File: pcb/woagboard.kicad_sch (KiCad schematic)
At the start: 54 parts, among them J1 TYPE-C-31-M-12, J2 SWD, J3 TC2030, SW1 SW_Push_45deg, SW10 SW_Push_45deg, SW11 SW_Push_45deg, SW12 SW_Push_45deg, SW13 SW_Push_45deg, SW14 SW_Push_45deg, SW15 SW_Push_45deg, SW16 SW_Push_45deg, SW17 SW_Push_45deg, SW18 SW_Push_45deg, SW2 SW_Push_45deg, SW3 SW_Push_45deg, SW4 SW_Push_45deg, SW5 SW_Push_45deg, SW6 SW_Push_45deg, SW7 SW_Push_45deg, SW8 SW_Push_45deg, SW9 SW_Push_45deg, U1 E73-2G4M08S1C, U2 BQ24075RGT, U3 USBLC6-2, Y1 32.768kHz

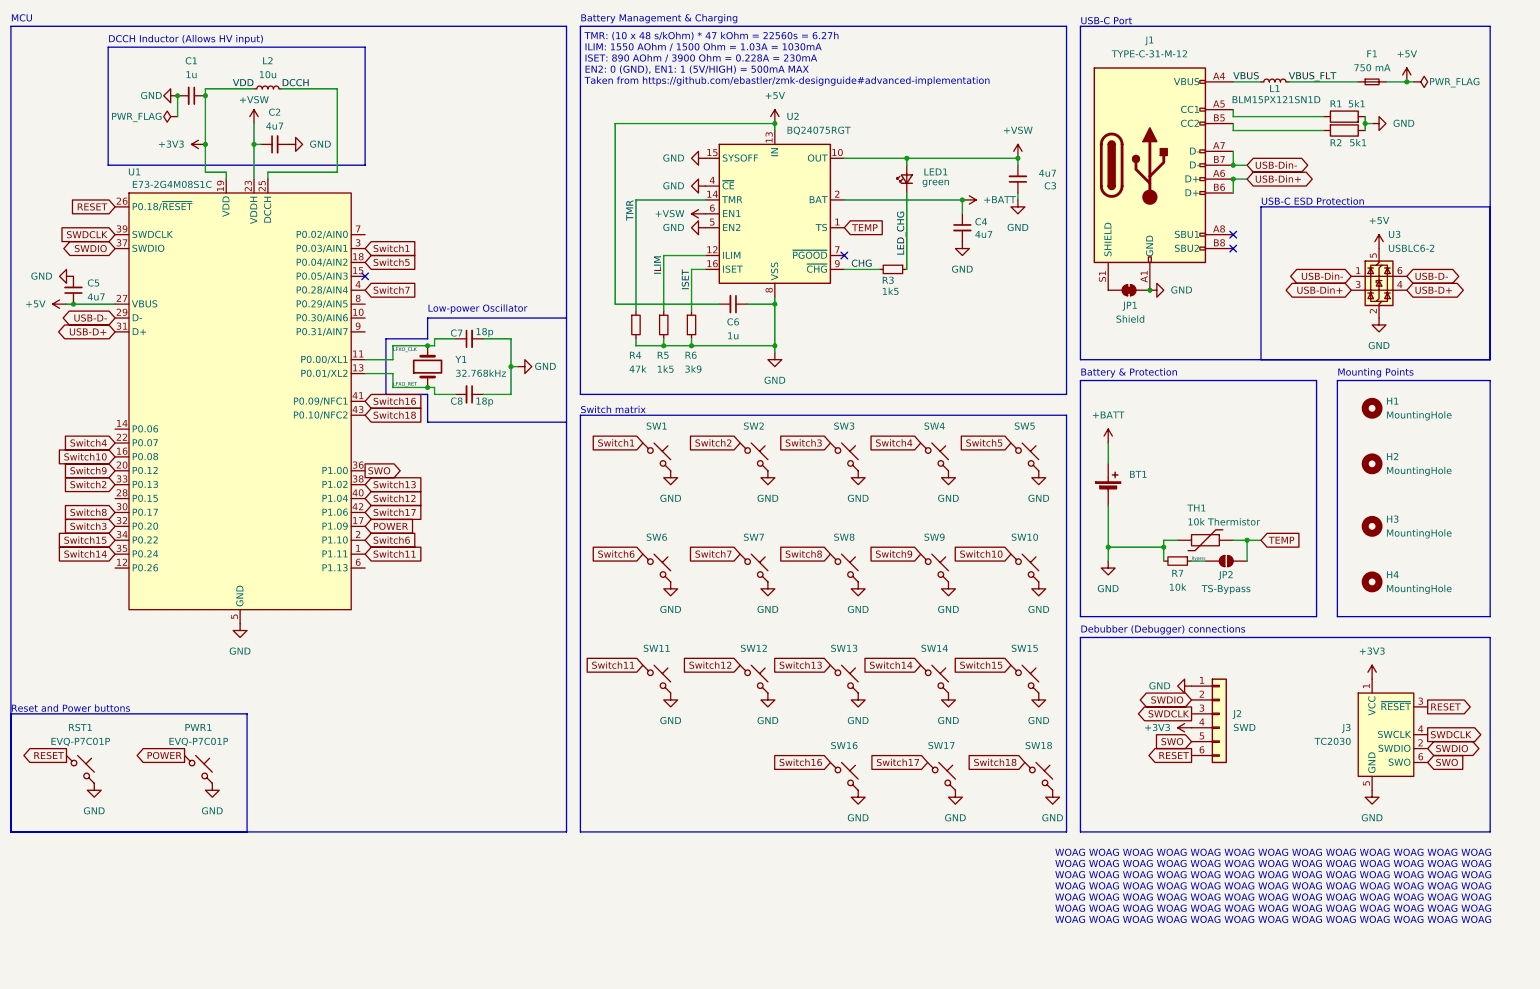
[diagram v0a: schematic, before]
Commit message: feat: reorganise and add basic case files
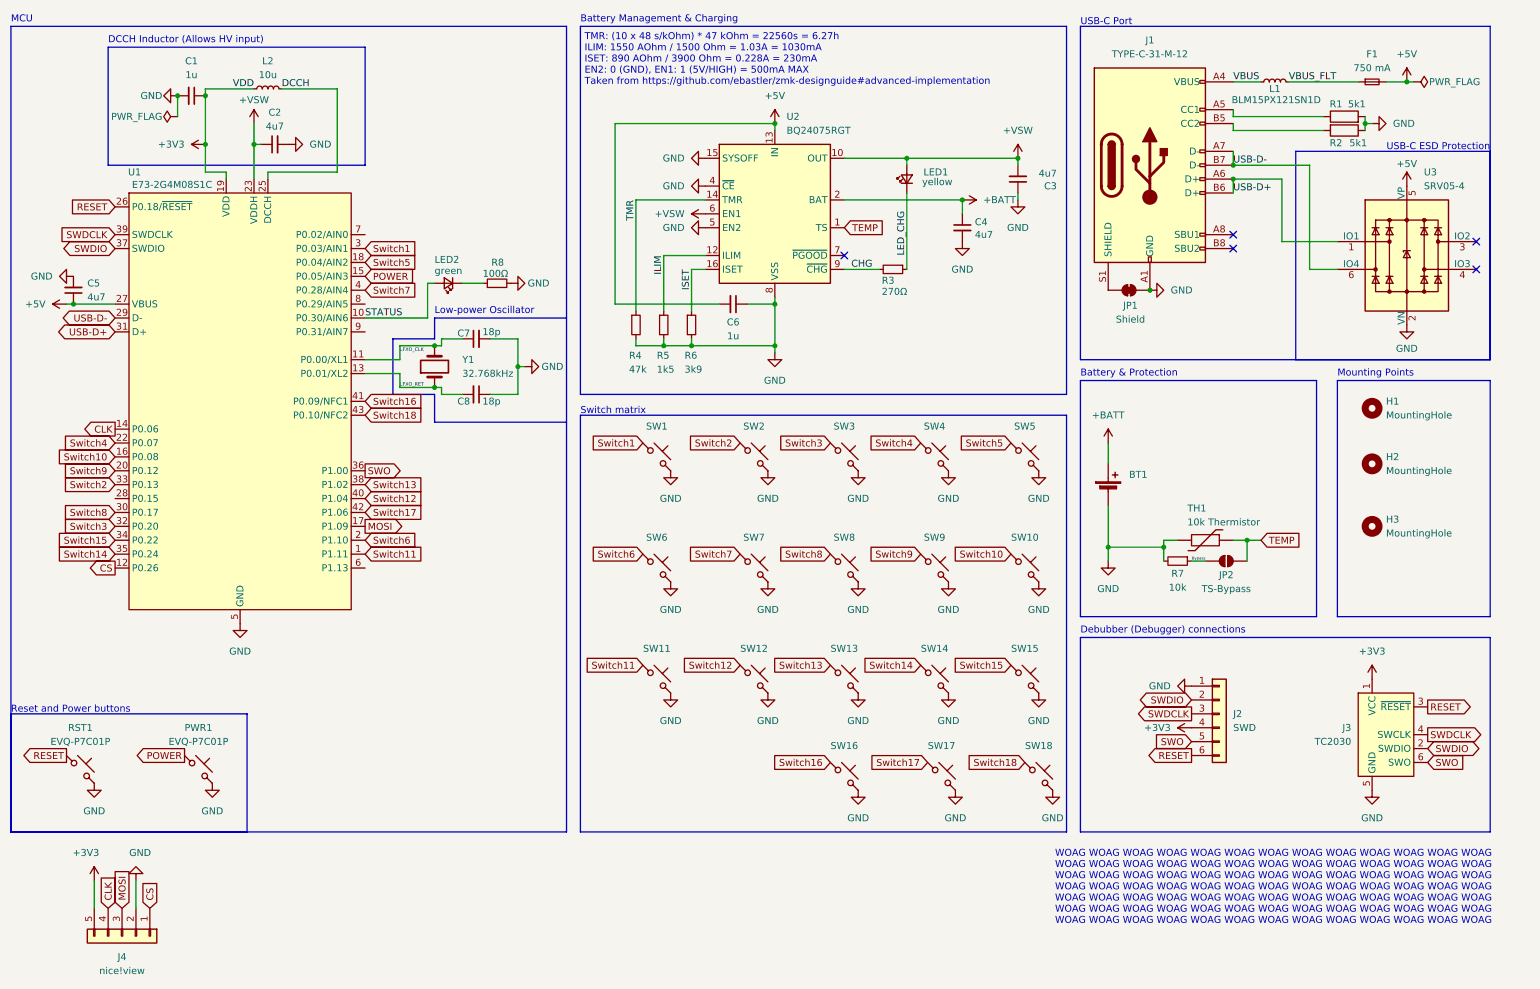
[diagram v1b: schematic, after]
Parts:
- removed H4: MountingHole, MountingHole:MountingHole_2.2mm_M2, symbol Mechanical:MountingHole
- removed U3: USBLC6-2, Package_TO_SOT_SMD:SOT-23-6_Handsoldering, symbol Power_Protection:USBLC6-2P6
- added J4: nice!view, Woagboard_Footprints:nice!view_pads, symbol Connector_Generic:Conn_01x05
- added LED2: green, LED_SMD:LED_0805_2012Metric_Pad1.15x1.40mm_HandSolder, symbol Device:LED_Small
- added R8: 100Ω, Resistor_SMD:R_0603_1608Metric_Pad0.98x0.95mm_HandSolder, symbol Device:R_Small
- added U3: SRV05-4, PCM_marbastlib-various:SOT-23-6-routable, symbol PCM_marbastlib-various:SRV05-4
- BT1, SW1, SW10, SW11, SW12, SW13, SW14, SW15, SW16, SW17, SW18, SW2, SW3, SW4, SW5, SW6, SW7, SW8, SW9: now left out of the parts list
- C1: LCSC (none) -> C52923
- C2, C5: LCSC (none) -> C23733
- C3, C4: LCSC C1538 -> C23733
- C7, C8: LCSC (none) -> C1549
- J1: LCSC (none) -> C165948
- J2: LCSC (none) -> C706869
- L2: LCSC (none) -> C223249
- LED1: value green -> yellow; footprint LED_SMD:LED_0603_1608Metric_Pad1.05x0.95mm_HandSolder -> LED_SMD:LED_0805_2012Metric_Pad1.15x1.40mm_HandSolder; LCSC C2290 -> C2296
- PWR1, RST1: LCSC (none) -> C388883
- R3: value 1k5 -> 270Ω; footprint Resistor_SMD:R_0402_1005Metric_Pad0.72x0.64mm_HandSolder -> Resistor_SMD:R_0603_1608Metric_Pad0.98x0.95mm_HandSolder
- U2: footprint Package_DFN_QFN:VQFN-16-1EP_3x3mm_P0.5mm_EP1.6x1.6mm -> Package_DFN_QFN:QFN-16-1EP_3x3mm_P0.5mm_EP1.7x1.7mm
- Y1: LCSC (none) -> C32346
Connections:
- net USB-Din+ is gone; now on net USB-D+: J1.A6 (D+), J1.B6 (D+)
- net USB-Din- is gone; now on net USB-D-: J1.A7 (D-), J1.B7 (D-)
- net +3V3: now also J4.5 (Pin_5)
- net +5V: now also U3.5 (VP)
- net GND: now also J4.2 (Pin_2), R8.2, U3.2 (VN)
- net POWER: now also U1.15 (P0.05/AIN3); no longer U1.17 (P1.09)
- net USB-D+: now also U3.1 (IO1)
- net USB-D-: now also U3.6 (IO4)
- net STATUS: now reaches U1.10 (P0.30/AIN6)
- net STATUS: now also LED2.2 (A)
- net CS: now reaches U1.12 (P0.26)
- net CS: now also J4.1 (Pin_1)
- net CLK: now reaches U1.14 (P0.06)
- net CLK: now also J4.4 (Pin_4)
- new net: LED2.1 (K), R8.1
- new net MOSI: J4.3 (Pin_3), U1.17 (P1.09)
- no-connect marks 4 -> 5
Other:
- moved on the sheet: C7, C8, Y1

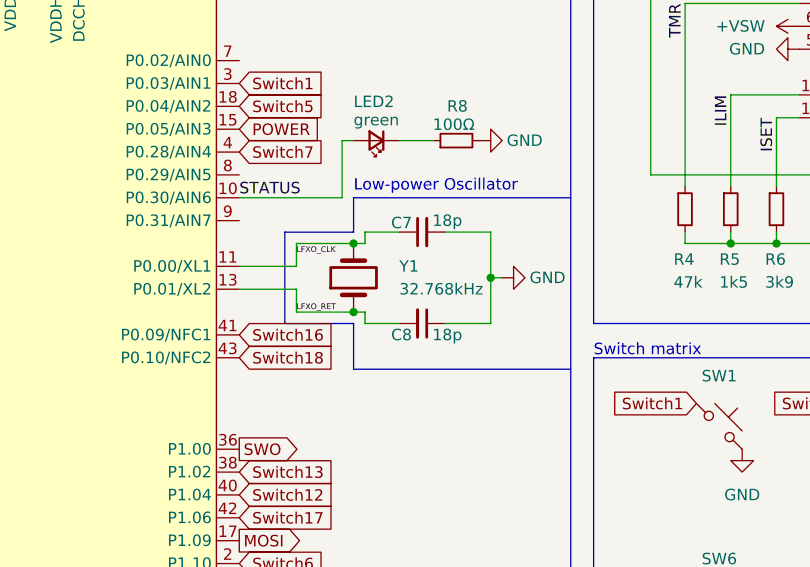
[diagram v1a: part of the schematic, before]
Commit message: feat: add rust firmware
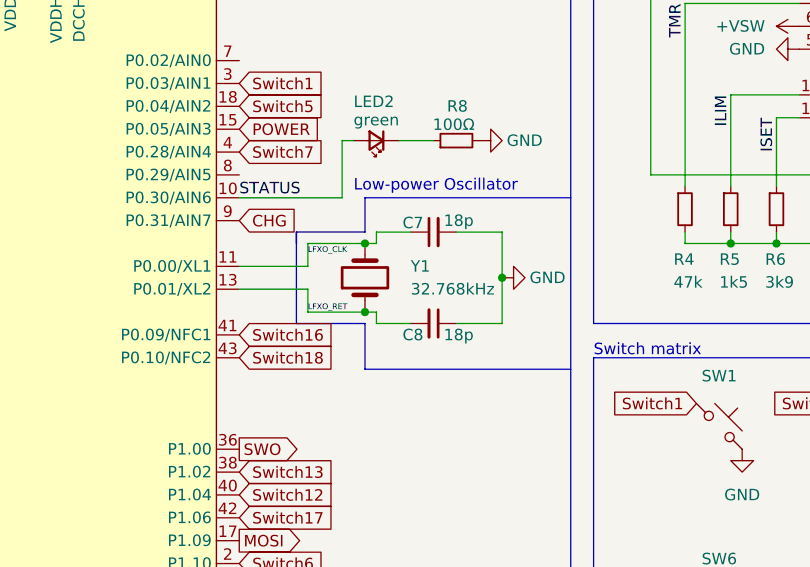
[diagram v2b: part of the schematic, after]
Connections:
- net CHG: now also U1.9 (P0.31/AIN7)
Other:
- moved on the sheet: C7, C8, Y1
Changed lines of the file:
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@@
 	)
 	(junction
-		(at 91.44 74.93)
+		(at 92.71 74.93)
 		(diameter 0)
 		(color 0 0 0 0)
@@
 	)
 	(junction
-		(at 91.44 82.55)
+		(at 92.71 82.55)
 		(diameter 0)
 		(color 0 0 0 0)
@@
 	)
 	(junction
-		(at 106.68 78.74)
+		(at 107.95 78.74)
 		(diameter 0)
 		(color 0 0 0 0)
@@
 	(wire
 		(pts
-			(xy 106.68 78.74) (xy 106.68 73.66)
+			(xy 107.95 78.74) (xy 107.95 73.66)
 		)
 		(stroke
@@
 	(polyline
 		(pts
-			(xy 83.82 73.66) (xy 91.44 73.66)
+			(xy 85.09 73.66) (xy 92.71 73.66)
 		)
 		(stroke
@@
 	(wire
 		(pts
-			(xy 92.71 82.55) (xy 91.44 82.55)
+			(xy 93.98 82.55) (xy 92.71 82.55)
 		)
 		(stroke
@@
 	(polyline
 		(pts
-			(xy 91.44 88.9) (xy 115.57 88.9)
+			(xy 92.71 88.9) (xy 115.57 88.9)
 		)
 		(stroke
@@
 	(wire
 		(pts
-			(xy 101.6 83.82) (xy 106.68 83.82)
+			(xy 102.87 83.82) (xy 107.95 83.82)
 		)
 		(stroke
@@
 	(polyline
 		(pts
-			(xy 91.44 83.82) (xy 91.44 88.9)
+			(xy 92.71 83.82) (xy 92.71 88.9)
 		)
 		(stroke
@@
 	(wire
 		(pts
-			(xy 85.09 77.47) (xy 85.09 74.93)
+			(xy 86.36 77.47) (xy 86.36 74.93)
 		)
 		(stroke
@@
 	(wire
 		(pts
-			(xy 78.74 80.01) (xy 85.09 80.01)
+			(xy 78.74 80.01) (xy 86.36 80.01)
 		)
 		(stroke
@@
 	(wire
 		(pts
-			(xy 85.09 80.01) (xy 85.09 82.55)
+			(xy 86.36 80.01) (xy 86.36 82.55)
 		)
 		(stroke
@@
 		)
 	)
+	(polyline
+		(pts
+			(xy 85.09 73.66) (xy 85.09 74.93)
+		)
+		(stroke
+			(width 0)
+			(type default)
+		)
+	)
 	(wire
 		(pts
@@
 	(wire
 		(pts
-			(xy 92.71 83.82) (xy 96.52 83.82)
+			(xy 93.98 83.82) (xy 97.79 83.82)
 		)
 		(stroke
@@
 	(wire
 		(pts
-			(xy 92.71 73.66) (xy 96.52 73.66)
+			(xy 93.98 73.66) (xy 97.79 73.66)
 		)
 		(stroke
@@
 	(wire
 		(pts
-			(xy 106.68 83.82) (xy 106.68 78.74)
+			(xy 107.95 83.82) (xy 107.95 78.74)
 		)
 		(stroke
@@
 	(wire
 		(pts
-			(xy 92.71 82.55) (xy 92.71 83.82)
+			(xy 93.98 82.55) (xy 93.98 83.82)
 		)
 		(stroke
@@
 	(wire
 		(pts
-			(xy 92.71 74.93) (xy 91.44 74.93)
+			(xy 93.98 74.93) (xy 92.71 74.93)
 		)
 		(stroke
@@
 	(wire
 		(pts
-			(xy 85.09 74.93) (xy 91.44 74.93)
+			(xy 86.36 74.93) (xy 92.71 74.93)
 		)
 		(stroke
@@
 	(wire
 		(pts
-			(xy 78.74 77.47) (xy 85.09 77.47)
+			(xy 78.74 77.47) (xy 86.36 77.47)
 		)
 		(stroke
@@
 	(polyline
 		(pts
-			(xy 91.44 73.66) (xy 91.44 69.85)
+			(xy 92.71 73.66) (xy 92.71 69.85)
 		)
 		(stroke
@@
 	(wire
 		(pts
-			(xy 106.68 73.66) (xy 101.6 73.66)
+			(xy 107.95 73.66) (xy 102.87 73.66)
 		)
 		(stroke
@@
 	(wire
 		(pts
-			(xy 92.71 74.93) (xy 92.71 73.66)
+			(xy 93.98 74.93) (xy 93.98 73.66)
 		)
 		(stroke
@@
 	(wire
 		(pts
-			(xy 85.09 82.55) (xy 91.44 82.55)
+			(xy 86.36 82.55) (xy 92.71 82.55)
 		)
 		(stroke
@@
 	(polyline
 		(pts
-			(xy 91.44 69.85) (xy 115.57 69.85)
+			(xy 92.71 69.85) (xy 115.57 69.85)
 		)
 		(stroke
@@
 	(polyline
 		(pts
-			(xy 83.82 83.82) (xy 91.44 83.82)
-		)
-		(stroke
-			(width 0)
-			(type default)
-		)
-	)
-	(wire
-		(pts
-			(xy 107.95 78.74) (xy 106.68 78.74)
+			(xy 85.09 83.82) (xy 92.71 83.82)
 		)
 		(stroke
@@
 	(polyline
 		(pts
-			(xy 83.82 73.66) (xy 83.82 83.82)
+			(xy 85.09 73.66) (xy 85.09 83.82)
 		)
 		(stroke
@@
 	)
 	(label "LFXO_RET"
-		(at 85.09 82.55 0)
+		(at 86.36 82.55 0)
 		(effects
 			(font
@@
 	)
 	(label "LFXO_CLK"
-		(at 85.09 76.2 0)
+		(at 86.36 76.2 0)
 		(effects
 			(font
@@
 		)
 	)
+	(global_label "CHG"
+		(shape input)
+		(at 78.74 72.39 0)
+		(fields_autoplaced yes)
+		(effects
+			(font
+				(size 1.27 1.27)
+			)
+			(justify left)
+		)
+		(property "Intersheetrefs" "${INTERSHEET_REFS}"
+			(at 85.5957 72.39 0)
+			(effects
+				(font
+					(size 1.27 1.27)
+				)
+				(justify left)
+				(hide yes)
+			)
+		)
+	)
 	(global_label "Switch10"
 		(shape input)
@@
 	(symbol
 		(lib_id "Device:C_Small")
-		(at 99.06 73.66 90)
+		(at 100.33 73.66 90)
 		(unit 1)
 		(exclude_from_sim no)
@@
 		(dnp no)
 		(property "Reference" "C7"
-			(at 96.774 72.644 90)
+			(at 98.044 72.644 90)
 			(effects
 				(font
@@
 		)
 		(property "Value" "18p"
-			(at 101.854 72.39 90)
+			(at 103.124 72.39 90)
 			(effects
 				(font
@@
 		)
 		(property "Footprint" "Capacitor_SMD:C_0402_1005Metric_Pad0.74x0.62mm_HandSolder"
-			(at 99.06 73.66 0)
+			(at 100.33 73.66 0)
 			(effects
 				(font
@@
 		)
 		(property "Datasheet" "~"
-			(at 99.06 73.66 0)
+			(at 100.33 73.66 0)
 			(effects
 				(font
@@
 		)
 		(property "Description" "Unpolarized capacitor, small symbol"
-			(at 99.06 73.66 0)
+			(at 100.33 73.66 0)
 			(effects
 				(font
@@
 		)
 		(property "LCSC" "C1549"
-			(at 96.774 72.644 0)
+			(at 98.044 72.644 0)
 			(effects
 				(font
@@
 	(symbol
 		(lib_id "Device:C_Small")
-		(at 99.06 83.82 270)
+		(at 100.33 83.82 270)
 		(unit 1)
 		(exclude_from_sim no)
@@
 		(dnp no)
 		(property "Reference" "C8"
-			(at 96.774 85.09 90)
+			(at 98.044 85.09 90)
 			(effects
 				(font
@@
 		)
 		(property "Value" "18p"
-			(at 101.854 85.09 90)
+			(at 103.124 85.09 90)
 			(effects
 				(font
@@
 		)
 		(property "Footprint" "Capacitor_SMD:C_0402_1005Metric_Pad0.74x0.62mm_HandSolder"
-			(at 99.06 83.82 0)
+			(at 100.33 83.82 0)
 			(effects
 				(font
@@
 		)
 		(property "Datasheet" "~"
-			(at 99.06 83.82 0)
+			(at 100.33 83.82 0)
 			(effects
 				(font
@@
 		)
 		(property "Description" "Unpolarized capacitor, small symbol"
-			(at 99.06 83.82 0)
+			(at 100.33 83.82 0)
 			(effects
 				(font
@@
 		)
 		(property "LCSC" "C1549"
-			(at 96.774 85.09 0)
+			(at 98.044 85.09 0)
 			(effects
 				(font
@@
 	(symbol
 		(lib_id "Device:Crystal")
-		(at 91.44 78.74 90)
+		(at 92.71 78.74 90)
 		(unit 1)
 		(exclude_from_sim no)
@@
 		(dnp no)
 		(property "Reference" "Y1"
-			(at 96.52 77.4699 90)
+			(at 97.79 77.4699 90)
 			(effects
 				(font
@@
 		)
 		(property "Value" "32.768kHz"
-			(at 96.52 80.0099 90)
+			(at 97.79 80.0099 90)
 			(effects
 				(font
@@
 		)
 		(property "Footprint" "Woagboard_Footprints:Q13FC13500004"
-			(at 91.44 78.74 0)
+			(at 92.71 78.74 0)
 			(effects
 				(font
@@
 		)
 		(property "Datasheet" "~"
-			(at 91.44 78.74 0)
+			(at 92.71 78.74 0)
 			(effects
 				(font
@@
 		)
 		(property "Description" "Two pin crystal"
-			(at 91.44 78.74 0)
+			(at 92.71 78.74 0)
 			(effects
 				(font
@@
 		)
 		(property "LCSC" "C32346"
-			(at 96.52 77.4699 0)
+			(at 97.79 77.4699 0)
 			(effects
 				(font

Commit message: feat: add renders
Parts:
- R3: value 270Ω -> 1k5
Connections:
- no-connect marks 5 -> 9
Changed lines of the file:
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@@
 	(text "Low-power Oscillator"
 		(exclude_from_sim no)
-		(at 91.44 69.342 0)
+		(at 92.71 69.596 0)
 		(effects
 			(font
@@
 	)
 	(no_connect
+		(at 33.02 102.87)
+	)
+	(no_connect
 		(at 166.37 58.42)
 	)
 	(no_connect
+		(at 78.74 67.31)
+	)
+	(no_connect
+		(at 78.74 54.61)
+	)
+	(no_connect
 		(at 281.94 55.88)
 	)
@@
 	)
 	(no_connect
+		(at 78.74 115.57)
+	)
+	(no_connect
 		(at 237.49 57.15)
 	)
@@
 			)
 		)
-		(property "Value" "270Ω"
+		(property "Value" "1k5"
 			(at 173.228 65.024 90)
 			(effects
